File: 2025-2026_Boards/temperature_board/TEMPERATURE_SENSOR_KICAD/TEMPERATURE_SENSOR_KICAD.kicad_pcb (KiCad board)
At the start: 2 copper layers, 73.3 x 75.8 mm, 89 parts, among them J1 LCD Connector Pinout, J10 Conn_01x02_Pin, J11 Conn_01x02_Pin, J12 Conn_01x02_Pin, J13 Conn_01x02_Pin, J14 Conn_01x02_Pin, J15 Conn_01x02_Pin, J16 Conn_01x02_Pin, J17 Conn_01x02_Pin, J18 Conn_01x02_Pin, J19 Conn_01x02_Pin, J2 Conn_01x02_Pin, J20 Conn_01x02_Pin, J21 Conn_01x02_Pin, J22 Conn_01x02_Pin, J23 Conn_01x02_Pin, J24 Conn_01x03_Socket, J25 Conn_01x03_Socket, J3 Conn_01x02_Pin, J4 Conn_01x02_Pin, J5 Conn_01x02_Pin, J6 Conn_01x02_Pin, J7 Conn_01x02_Pin, J8 Conn_01x02_Pin, J9 Conn_01x02_Pin, Q1 Q_NPN_BCE, Q3 Q_NPN_BCE, Q4 Q_NPN_BCE, Q5 Q_PNP_BCE, U1 STM32G431CBT6, U2 TMP235A4DBZR, U3 AMS1117-3.3, U4 TCAN1057AEV-Q1, U5 TPS62932DRLR

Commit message: rehashed
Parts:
- removed the TP1 at (97.5, 132.0)
- moved R1 39.1 mm to (127.8, 142.0), turned to 90 degrees
- moved D1 38.3 mm to (126.6, 142.5), turned to 180 degrees
- moved C2 38.2 mm to (127.6, 144.6), turned to 0 degrees
- moved TP1 38.2 mm to (128.2, 138.3)
- moved C1 29.5 mm to (117.6, 147.6)
- moved Rfbb1 29.4 mm to (98.2, 118.3)
- moved Cin4 28.6 mm to (92.5, 120.3), turned to -90 degrees
- moved L2 28.3 mm to (94.7, 130.0)
- moved Q4 28.0 mm to (127.7, 130.1), turned to -90 degrees
- moved Css2 27.4 mm to (98.7, 119.8), turned to 90 degrees
- moved U3 27.4 mm to (121.3, 142.0)
- moved Rfbt1 26.8 mm to (100.8, 121.2)
- moved U5 26.2 mm to (96.4, 120.7), turned to 0 degrees
- moved Q5 25.7 mm to (130.6, 130.1), turned to -90 degrees
- moved R10 25.2 mm to (128.4, 133.2), turned to 90 degrees
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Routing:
- net Net-(J1-Pin_12): track 83.0 -> 12.0 mm
- net Net-(U1-PA10): track 55.3 -> 3.04 mm
- net Net-(J1-Pin_8): track 61.1 -> 23.0 mm, vias 0 -> 4
- net Net-(J1-Pin_9): track 50.7 -> 13.9 mm
- net Net-(U1-PA8): track 40.5 -> 10.2 mm, vias 2 -> 0
- net 28V: track 58.7 -> 31.4 mm, vias 1 -> 0
- net Net-(J1-Pin_10): track 9.64 -> 34.6 mm, vias 0 -> 2
- net Net-(U1-PA7): track 21.9 -> 1.55 mm, vias 2 -> 0
- net Net-(J1-Pin_6): track 43.2 -> 26.1 mm
- net Net-(U1-PA14): track 12.9 -> 24.2 mm, vias 0 -> 4
- net Net-(U1-PA6): track 14.5 -> 23.1 mm, vias 0 -> 2
- net Net-(J1-Pin_11): track 17.5 -> 26.0 mm, vias 0 -> 4
- net Net-(Q3-B): track 1.65 -> 9.75 mm, vias 0 -> 4
- net Net-(U1-PA3): track 9.81 -> 3.07 mm
- net +3.3V: track 112.8 -> 119.0 mm, vias 10 -> 14
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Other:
- board text removed: "100n"

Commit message: rehashed
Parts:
- moved L2 12.1 mm to (91.3, 141.7)
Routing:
- net Net-(U5-SW): track 13.3 -> 26.7 mm
- net Net-(U1-PA8): track 10.2 -> 6.25 mm
- net 5V: track 220.2 -> 217.1 mm
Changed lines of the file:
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@@
 	(footprint "Inductor_SMD:L_Bourns_SRR1208_12.7x12.7mm"
 		(layer "F.Cu")
-		(at 94.66 130.04)
+		(at 91.2975 141.71)
 		(descr "Bourns SRP1208 series SMD inductor https://www.bourns.com/pdfs/SRR1208.pdf")
 		(tags "Bourns SRP1208 SMD inductor")
@@
 	)
 	(segment
-		(start 99.66 130.04)
-		(end 97.22 130.04)
-		(width 0.5)
-		(layer "F.Cu")
-		(net 8)
-	)
-	(segment
 		(start 105.25 162.75)
 		(end 105.25 163.2175)
@@
 	)
 	(segment
-		(start 97.22 130.04)
-		(end 87.51 139.75)
-		(width 0.5)
-		(layer "F.Cu")
-		(net 8)
-	)
-	(segment
 		(start 123.5 163.185)
 		(end 123.5 160.25)
@@
 	)
 	(segment
+		(start 96.2975 141.71)
+		(end 96.2975 133.4025)
+		(width 0.5)
+		(layer "F.Cu")
+		(net 8)
+	)
+	(segment
 		(start 143 131.4675)
 		(end 143 118.7825)
@@
 	)
 	(segment
+		(start 96.2975 133.4025)
+		(end 99.66 130.04)
+		(width 0.5)
+		(layer "F.Cu")
+		(net 8)
+	)
+	(segment
 		(start 120.904999 114.27)
 		(end 121.885 115.250001)
@@
 	)
 	(segment
+		(start 86.2975 141.71)
+		(end 86.2975 133.4025)
+		(width 0.5)
+		(layer "F.Cu")
+		(net 51)
+	)
+	(segment
+		(start 89.89 129.81)
+		(end 89.66 130.04)
+		(width 0.3)
+		(layer "F.Cu")
+		(net 51)
+	)
+	(segment
 		(start 97.2409 121.460189)
 		(end 98.695189 121.460189)
@@
 	)
 	(segment
+		(start 86.2975 133.4025)
+		(end 89.89 129.81)
+		(width 0.5)
+		(layer "F.Cu")
+		(net 51)
+	)
+	(segment
 		(start 97.2409 122.4591)
-		(end 89.66 130.04)
+		(end 89.89 129.81)
 		(width 0.3)
 		(layer "F.Cu")
@@
 		(width 0.2)
 		(layer "F.Cu")
-		(net 68)
-	)
-	(segment
-		(start 125.96 127)
-		(end 123.16 124.2)
-		(width 0.2)
-		(layer "F.Cu")

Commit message: rehashed
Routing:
- net 5V: track 217.1 -> 226.7 mm
- net Net-(U1-PA8): track 6.25 -> 10.2 mm
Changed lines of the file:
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@@
+	)
+	(segment
+		(start 96.2975 141.71)
+		(end 96.2975 151.1625)
+		(width 0.5)
+		(layer "F.Cu")
+		(net 8)
 	)
 	(segment
@@
 		(start 82.75 130.25)
 		(end 83 130)
+		(width 0.5)
+		(layer "F.Cu")
+		(net 8)
+	)
+	(segment
+		(start 96.2975 151.1625)
+		(end 96.2 151.26)
 		(width 0.5)
 		(layer "F.Cu")
@@
 	)
 	(segment
-		(start 86.2975 141.71)
-		(end 86.2975 133.4025)
-		(width 0.5)
-		(layer "F.Cu")
-		(net 51)
-	)
-	(segment
-		(start 89.89 129.81)
-		(end 89.66 130.04)
+		(start 97.2409 124.0791)
+		(end 97.2409 121.460189)
 		(width 0.3)
 		(layer "F.Cu")
@@
 	)
 	(segment
-		(start 86.2975 133.4025)
-		(end 89.89 129.81)
-		(width 0.5)
-		(layer "F.Cu")
-		(net 51)
-	)
-	(segment
-		(start 97.2409 122.4591)
-		(end 89.89 129.81)
-		(width 0.3)
-		(layer "F.Cu")
-		(net 51)
-	)
-	(segment
-		(start 97.2409 121.460189)
-		(end 97.2409 122.4591)
+		(start 86.2975 135.0225)
+		(end 97.2409 124.0791)
 		(width 0.3)
 		(layer "F.Cu")
@@
 	)
 	(segment
+		(start 86.2975 141.71)
+		(end 86.2975 135.0225)
+		(width 0.3)
+		(layer "F.Cu")
+		(net 51)
+	)
+	(segment
 		(start 97.2409 120.960063)
 		(end 98.724937 120.960063)
@@
 	)
 	(segment
+		(start 116.9125 124.2)
+		(end 123.16 124.2)
+		(width 0.2)
+		(layer "F.Cu")
+		(net 68)
+	)
+	(segment
 		(start 123.16 124.2)
-		(end 116.9125 124.2)
-		(width 0.2)
-		(layer "F.Cu")
+		(end 125.96 127)
+		(width 0.2)
+		(layer "F.Cu")

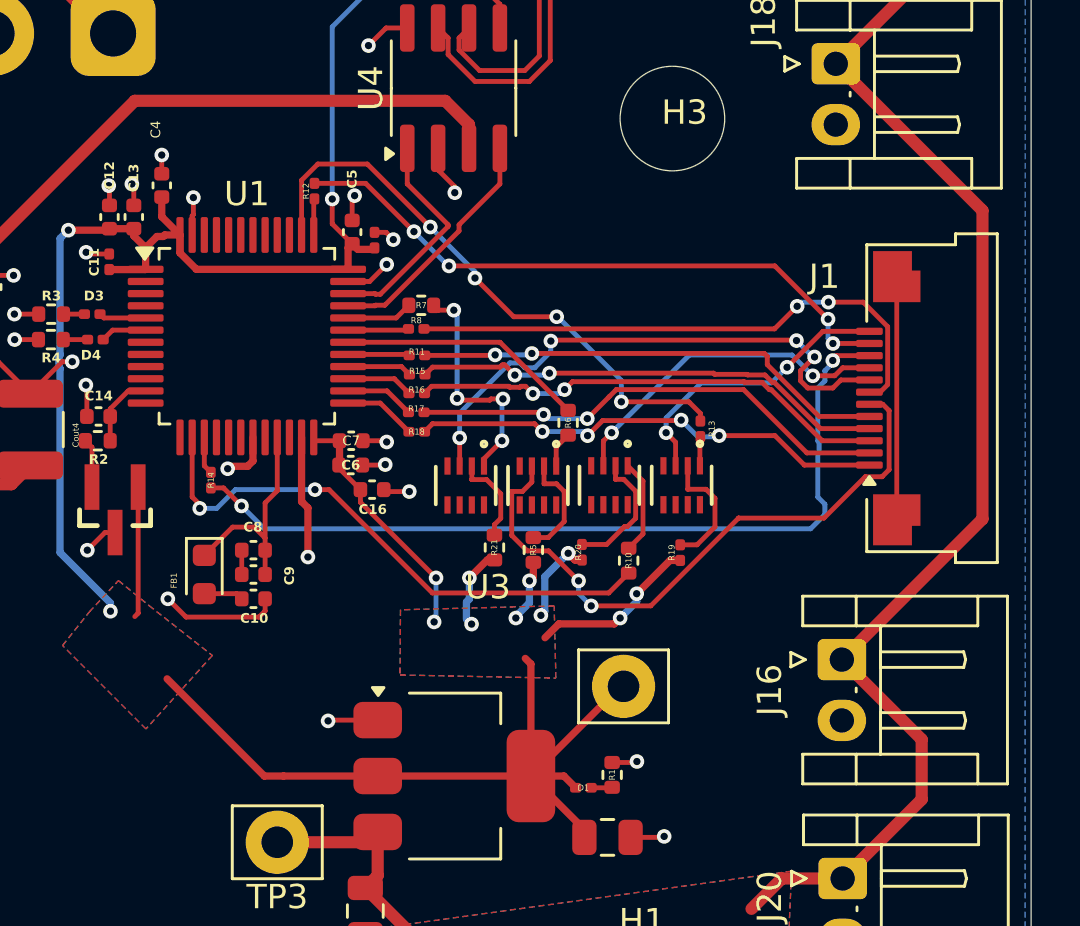
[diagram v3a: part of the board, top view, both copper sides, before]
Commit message: reduced #vias
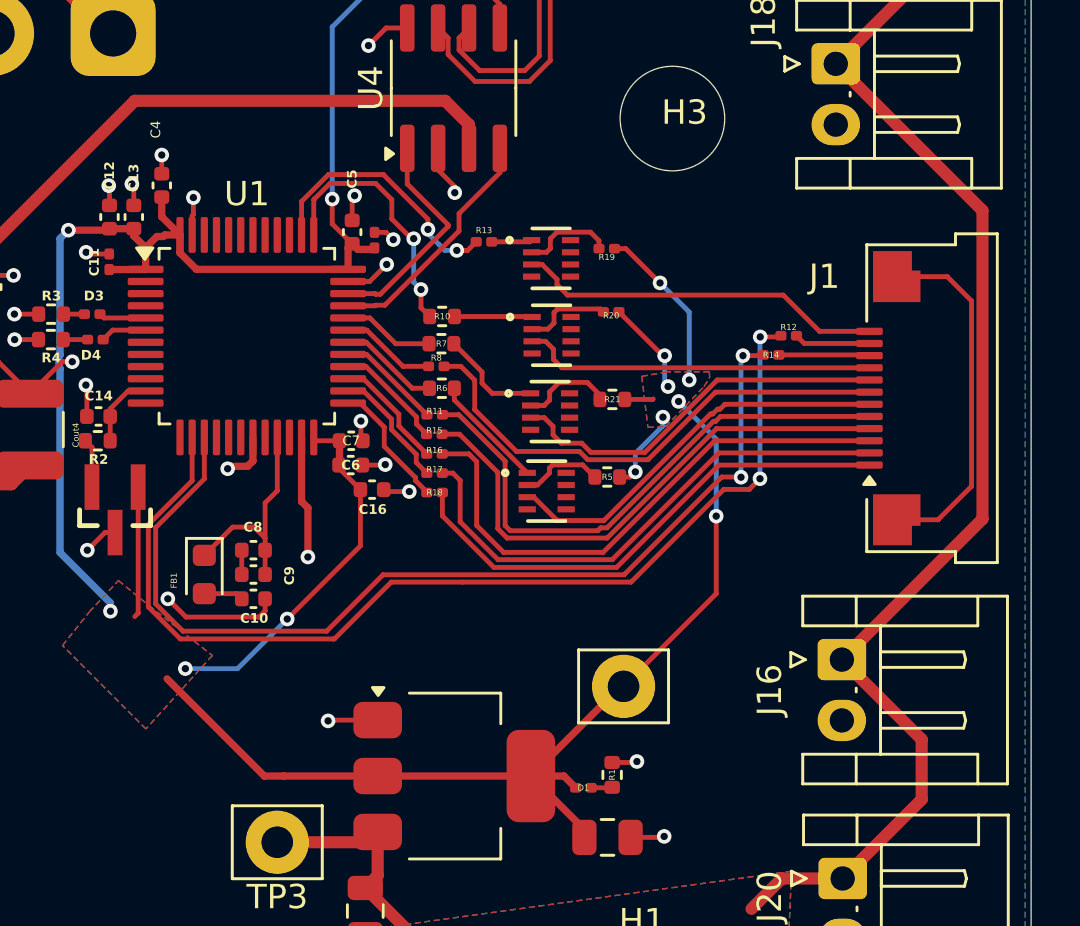
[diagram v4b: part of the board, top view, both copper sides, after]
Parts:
- moved R14 23.6 mm to (134.3, 124.7), turned to 0 degrees
- moved R12 20.4 mm to (135.0, 123.9), turned to 0 degrees
- moved R19 12.9 mm to (127.5, 120.3), turned to 180 degrees
- moved R10 12.6 mm to (120.8, 123.1), turned to 0 degrees
- moved R13 11.8 mm to (122.5, 120.1), turned to 0 degrees
- moved Q5 10.8 mm to (125.3, 120.8), turned to 0 degrees
- moved R20 9.96 mm to (127.7, 123.0), turned to 180 degrees
- moved R21 7.79 mm to (127.8, 126.5), turned to 180 degrees
- moved Q4 6.61 mm to (125.3, 123.9), turned to 0 degrees
- moved R6 5.38 mm to (120.8, 126.1), turned to 0 degrees
- moved Q3 4.61 mm to (125.2, 127.0), turned to 0 degrees
- moved R5 4.27 mm to (127.6, 129.7), turned to 180 degrees
- moved R17 2.61 mm to (120.5, 129.6)
- moved R18 2.61 mm to (120.5, 130.4)
- moved R16 2.59 mm to (120.5, 128.8)
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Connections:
- R10 pad 1: Net-(U1-PA6) -> Net-(U1-PA13)
- R12 pad 1: Net-(U1-PA13) -> Net-(U1-PA6)
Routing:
- net Net-(U1-PA7): track 1.55 -> 40.7 mm, vias 0 -> 2
- net Net-(J1-Pin_10): track 34.6 -> 3.74 mm, vias 2 -> 0
- net Net-(J1-Pin_11): track 26.0 -> 3.13 mm, vias 4 -> 0
- net Net-(U1-PA6): track 23.1 -> 42.8 mm
- net Net-(U1-PA14): track 24.2 -> 10.8 mm, vias 4 -> 2
- net +3.3V: track 119.0 -> 131.6 mm
- net Net-(J1-Pin_6): track 26.1 -> 16.5 mm, vias 2 -> 0
- net Net-(U1-PA13): track 1.49 -> 10.7 mm, vias 0 -> 2
- net Net-(J1-Pin_8): track 23.0 -> 16.0 mm, vias 4 -> 0
- net Net-(U1-PA8): track 10.2 -> 4.13 mm
- net Net-(Q3-B): track 9.75 -> 4.28 mm, vias 4 -> 0
- net unconnected-(J1-MountPin-PadMP): track 10.0 -> 14.8 mm
- net Net-(J1-Pin_5): track 19.6 -> 23.0 mm, vias 2 -> 0
- net Net-(Q1-B): track 1.47 -> 4.72 mm
- net Net-(J1-Pin_12): track 12.0 -> 15.2 mm, vias 2 -> 0
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
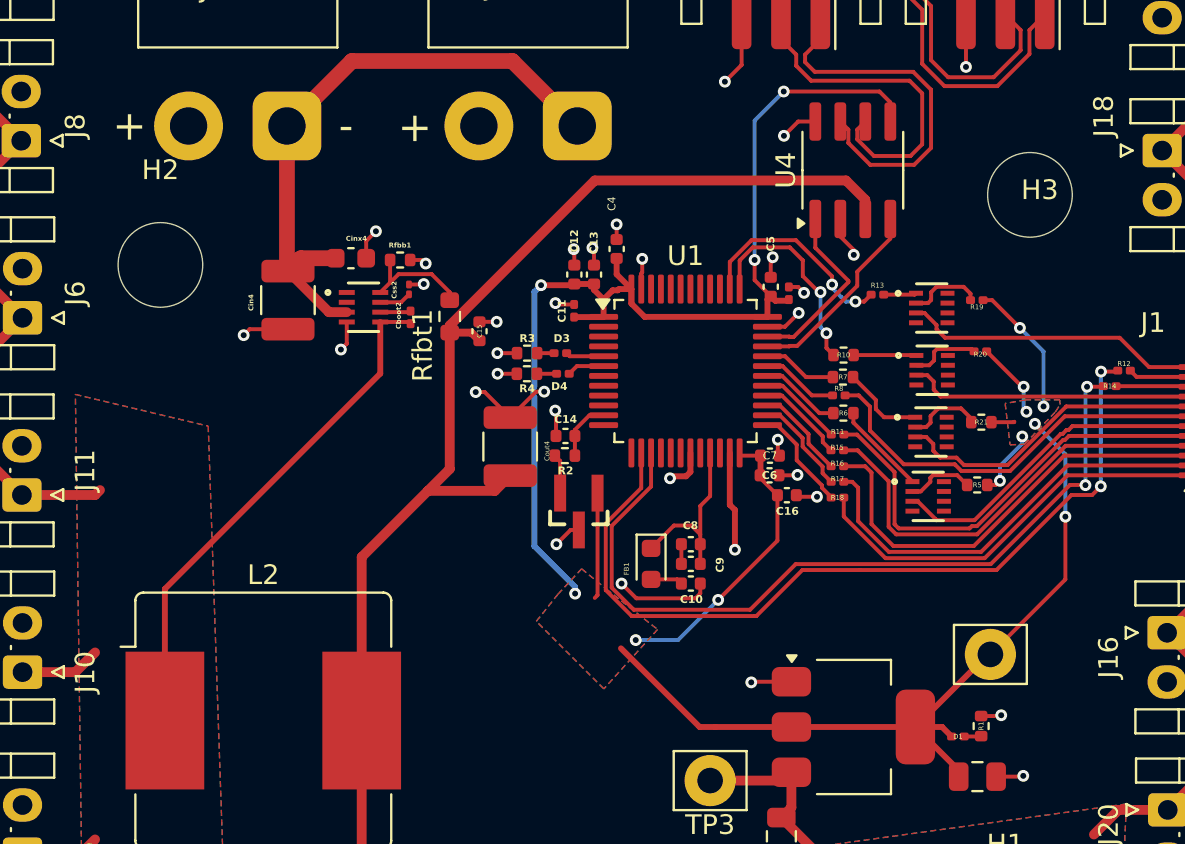
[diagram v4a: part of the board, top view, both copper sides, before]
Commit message: moved 5v regulator closer
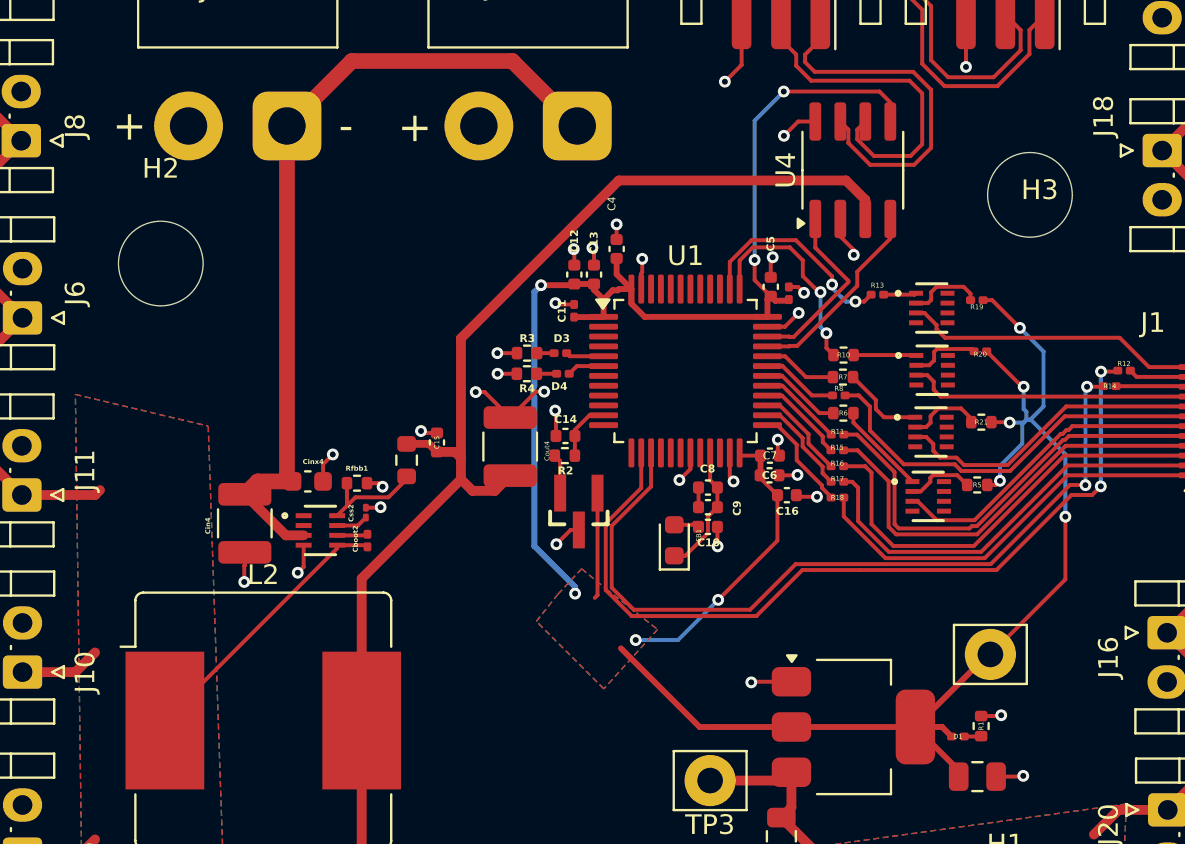
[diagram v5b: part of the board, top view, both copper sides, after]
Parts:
- moved Cboot2 11.5 mm to (96.6, 132.6)
- moved Cin4 11.5 mm to (90.4, 131.7)
- moved Cinx4 11.5 mm to (93.6, 129.6)
- moved U5 11.5 mm to (94.2, 132.1)
- moved Css2 11.5 mm to (96.5, 131.1)
- moved Rfbb1 11.5 mm to (96.1, 129.7)
- moved Rfbt1 7.63 mm to (98.6, 128.5), turned to -90 degrees
- moved C15 6.05 mm to (100.1, 127.6)
- moved C10 3.01 mm to (113.9, 131.9)
- moved C8 3.01 mm to (113.9, 129.9)
- moved C9 3.01 mm to (113.9, 130.9)
- moved FB1 1.68 mm to (112.2, 132.6), turned to 90 degrees
- moved H2 0.07 mm to (86.1, 118.5)
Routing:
- net Net-(U5-SW): track 26.4 -> 14.1 mm
- net 28V: track 31.4 -> 42.3 mm
- net GND: track 57.8 -> 49.0 mm
- net +3.3V: track 131.6 -> 135.2 mm, vias 14 -> 11
- net +3.3VA: track 9.01 -> 6.61 mm
- net 5V: track 226.7 -> 225.9 mm
